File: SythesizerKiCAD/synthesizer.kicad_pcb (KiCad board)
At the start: 2 copper layers, 98.2 x 95.2 mm, 42 parts, among them U2 LM1877, U3 LM324A

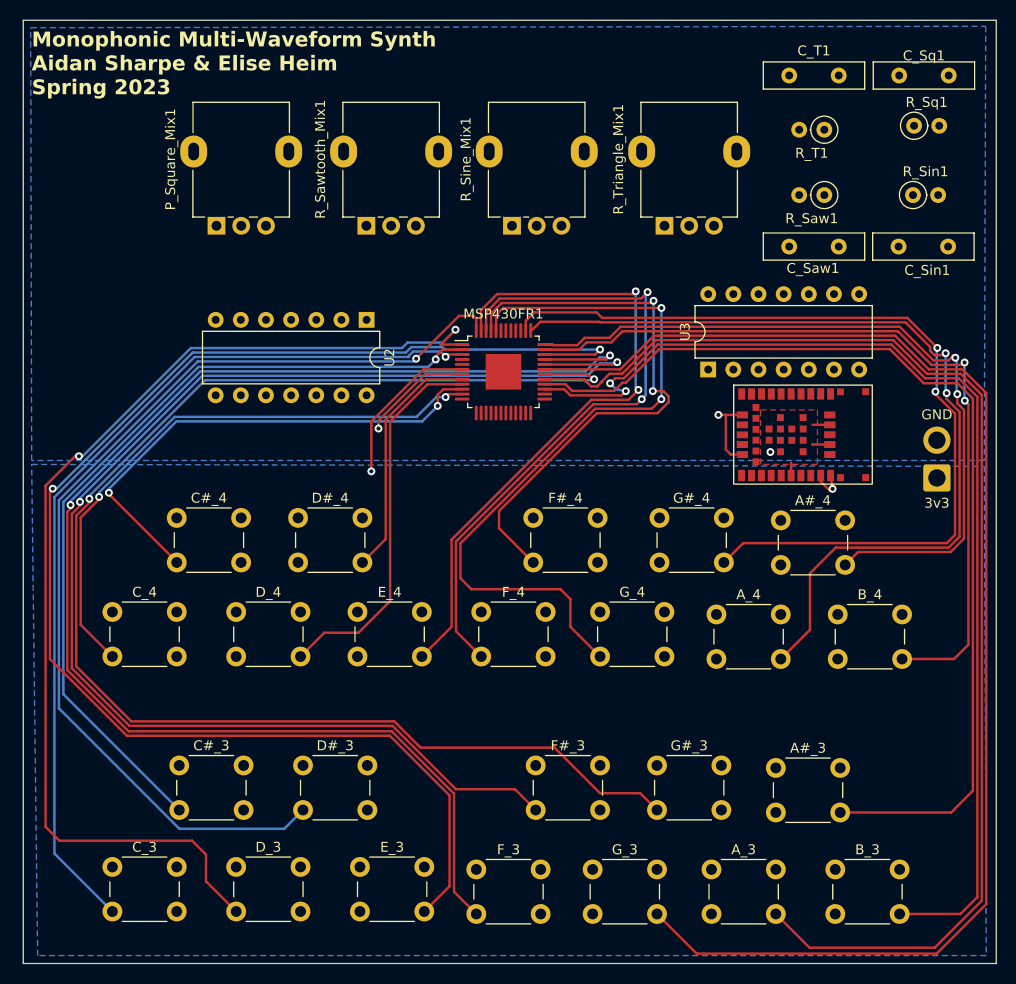
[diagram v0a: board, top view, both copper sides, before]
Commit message: Lowpass filters and isolators
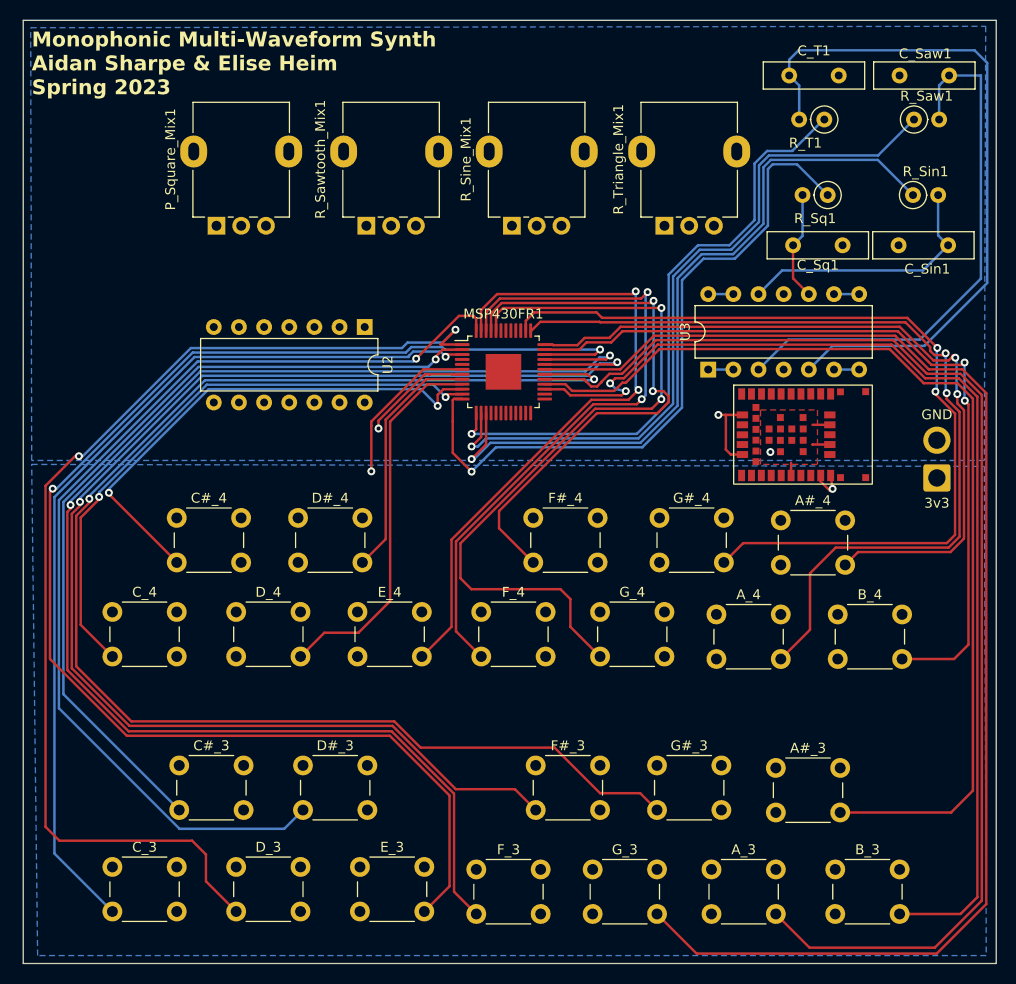
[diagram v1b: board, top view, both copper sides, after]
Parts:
- moved C_Saw1 23.6 mm to (121.2, 60.3), turned to 180 degrees
- moved C_Sq1 23.3 mm to (105.5, 77.5), turned to 0 degrees
- moved R_Saw1 11.8 mm to (117.7, 64.8), turned to 0 degrees
- moved R_Sq1 11.2 mm to (109.0, 72.4), turned to 180 degrees
- moved R_T1 1.03 mm to (108.6, 64.8)
- moved U2 0.75 mm to (62.2, 85.7)
- moved C_Sin1 0.13 mm to (121.1, 77.5)
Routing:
- net /Sine_PWM: track 0.00 -> 74.7 mm, vias 0 -> 1
- net /Sawtooth_PWM: track 0.00 -> 73.0 mm, vias 0 -> 1
- net /Triangle_Analog: track 0.00 -> 71.2 mm
- net /Square_PWM: track 0.00 -> 70.0 mm, vias 0 -> 1
- net /Triangle_PWM: track 0.00 -> 62.0 mm, vias 0 -> 1
- net /Sawtooth_Analog: track 0.00 -> 54.8 mm
- net /Sine_Analog: track 0.00 -> 26.7 mm
- net /Square_Analog: track 0.00 -> 11.1 mm
- net /Triangle_Isolated: track 0.00 -> 2.54 mm
- net /Square_Isolated: track 0.00 -> 2.54 mm
- net /Sine_Isolated: track 0.00 -> 2.54 mm
- net /Sawtooth_Isolated: track 0.00 -> 2.54 mm
- net /P2.5: track 50.8 -> 52.2 mm
- net /P2.4: track 59.5 -> 60.6 mm

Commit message: Volume, audio out, power in
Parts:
- removed GND: SolderWire-1sqmm_1x01_D1.4mm_OD2.7mm, Connector_Wire:SolderWire-1sqmm_1x01_D1.4mm_OD2.7mm
- added 9v1: Conn_01x01_Pin, Connector_Wire:SolderWire-0.1sqmm_1x01_D0.4mm_OD1mm, F.Cu at (29.8, 96.6)
- added Audio_Out1: Conn_01x01_Pin, Connector_Wire:SolderWire-0.1sqmm_1x01_D0.4mm_OD1mm, F.Cu at (30.0, 70.6)
- added GND1: Conn_01x01_Pin, Connector_Wire:SolderWire-0.1sqmm_1x01_D0.4mm_OD1mm, F.Cu at (29.8, 93.2)
- added GND2: Conn_01x01_Pin, Connector_Wire:SolderWire-0.1sqmm_1x01_D0.4mm_OD1mm, F.Cu at (30.0, 66.4)
- added R1: 100k, Resistor_THT:R_Axial_DIN0207_L6.3mm_D2.5mm_P2.54mm_Vertical, F.Cu at (87.8, 75.5)
- added R2: 300k, Resistor_THT:R_Axial_DIN0207_L6.3mm_D2.5mm_P2.54mm_Vertical, F.Cu at (91.0, 78.0)
- added R3: 300k, Resistor_THT:R_Axial_DIN0207_L6.3mm_D2.5mm_P2.54mm_Vertical, F.Cu at (42.7, 78.2)
- added R4: 100k, Resistor_THT:R_Axial_DIN0207_L6.3mm_D2.5mm_P2.54mm_Vertical, F.Cu at (39.5, 75.6)
- added R5: 300k, Resistor_THT:R_Axial_DIN0207_L6.3mm_D2.5mm_P2.54mm_Vertical, F.Cu at (74.9, 78.2)
- added R6: 100k, Resistor_THT:R_Axial_DIN0207_L6.3mm_D2.5mm_P2.54mm_Vertical, F.Cu at (71.7, 75.6)
- added R7: 300k, Resistor_THT:R_Axial_DIN0207_L6.3mm_D2.5mm_P2.54mm_Vertical, F.Cu at (58.8, 78.3)
- added R8: 100k, Resistor_THT:R_Axial_DIN0207_L6.3mm_D2.5mm_P2.54mm_Vertical, F.Cu at (55.7, 75.7)
- added R9: 100k, Resistor_THT:R_Axial_DIN0207_L6.3mm_D2.5mm_P2.54mm_Vertical, F.Cu at (33.1, 74.6)
- added R_Volume1: R_Potentiometer_US, Potentiometer_THT:Potentiometer_Alpha_RD901F-40-00D_Single_Vertical, F.Cu at (32.1, 89.9)
- 3v3: value SolderWire-1sqmm_1x01_D1.4mm_OD2.7mm -> Conn_01x01_Pin; footprint Connector_Wire:SolderWire-1sqmm_1x01_D1.4mm_OD2.7mm -> Connector_Wire:SolderWire-0.1sqmm_1x01_D0.4mm_OD1mm
- U3: value LM324A -> LMC6484
- moved 3v3 90.2 mm to (29.8, 103.0)
- moved P_Square_Mix1 46.2 mm to (93.4, 73.2)
- moved R_Sine_Mix1 32.1 mm to (45.1, 73.3)
- moved R_Triangle_Mix1 15.4 mm to (77.3, 73.2)
- moved R_Sawtooth_Mix1 2.40 mm to (61.2, 73.4)
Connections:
- P_Square_Mix1 pad 1: unconnected-(P_Square_Mix1-Pad1) -> /Square_Divided
- P_Square_Mix1 pad 2: unconnected-(P_Square_Mix1-Pad2) -> /Mixed
- R_Sawtooth_Mix1 pad 1: unconnected-(R_Sawtooth_Mix1-Pad1) -> /Sawtooth_Divided
- R_Sawtooth_Mix1 pad 2: unconnected-(R_Sawtooth_Mix1-Pad2) -> /Mixed
- R_Sine_Mix1 pad 1: unconnected-(R_Sine_Mix1-Pad1) -> /Sine_Divided
- R_Sine_Mix1 pad 2: unconnected-(R_Sine_Mix1-Pad2) -> /Mixed
- R_Triangle_Mix1 pad 1: unconnected-(R_Triangle_Mix1-Pad1) -> /Triangle_Divided
- R_Triangle_Mix1 pad 2: unconnected-(R_Triangle_Mix1-Pad2) -> /Mixed
- U1 pad 42: /GND -> (no net)
- U2 pad 14: /12v -> /9v
- U2 pad 2: unconnected-(U2-Pad2) -> /Audio_Out
- U2 pad 6: unconnected-(U2A-+-Pad6) -> /Mixed
- U2 pad 7: unconnected-(U2A---Pad7) -> Net-(U2A--)
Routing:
- net /Mixed: track 0.00 -> 67.6 mm
- net /Sine_Isolated: track 2.54 -> 58.5 mm
- net /Sawtooth_Isolated: track 2.54 -> 55.0 mm, vias 0 -> 1
- net /Triangle_Isolated: track 2.54 -> 51.6 mm, vias 0 -> 1
- net /Audio_Out: track 0.00 -> 48.1 mm
- net /9v: track 0.00 -> 34.0 mm
- net Net-(U2A--): track 0.00 -> 31.0 mm
- net /Square_Isolated: track 2.54 -> 24.7 mm
- net /GND: track 23.4 -> 36.0 mm, vias 3 -> 5
- net /Sawtooth_Analog: track 54.8 -> 47.2 mm
- net /Square_Divided: track 0.00 -> 6.57 mm
- net /Sine_Divided: track 0.00 -> 6.57 mm
- net /Triangle_Divided: track 0.00 -> 6.57 mm
- net /Sawtooth_Divided: track 0.00 -> 6.46 mm
- net unconnected-(U1-GPI_15-Pad15): track 0.00 -> 5.20 mm
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
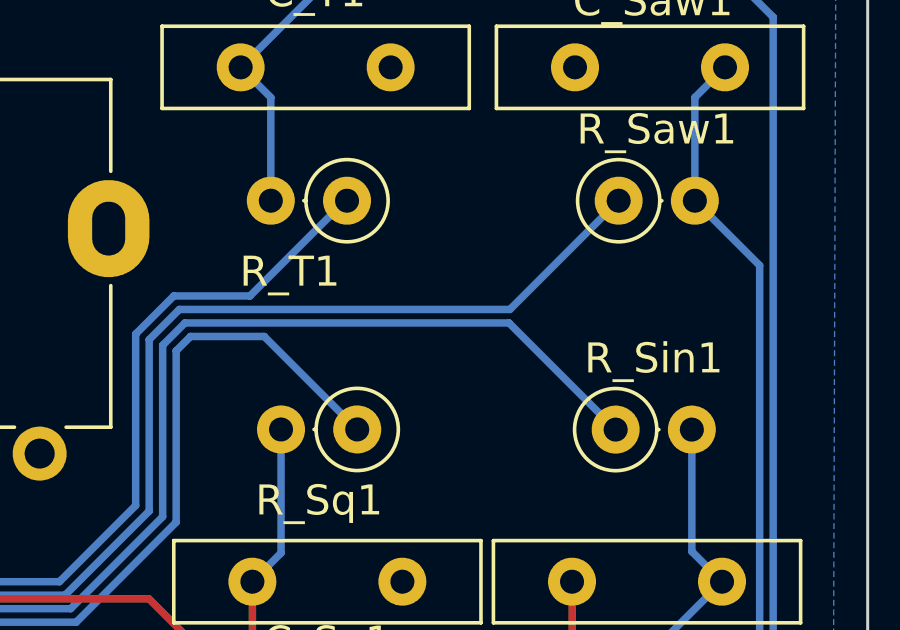
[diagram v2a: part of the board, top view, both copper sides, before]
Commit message: Fixed ground issue
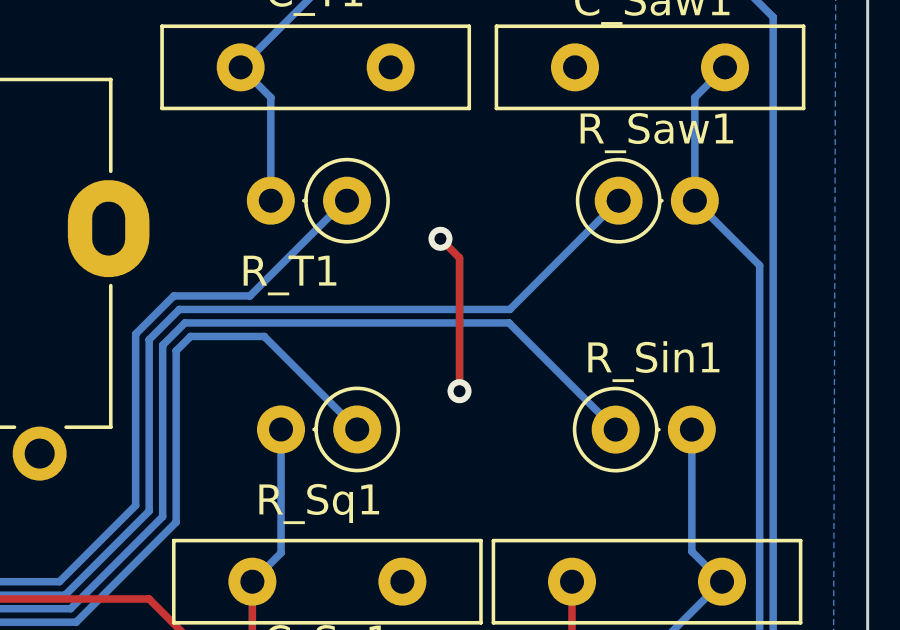
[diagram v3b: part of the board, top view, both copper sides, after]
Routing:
- net /GND: track 36.0 -> 41.4 mm, vias 5 -> 7
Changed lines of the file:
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@@
   (segment (start 71.03 90.5) (end 71.04 90.51) (width 0.25) (layer "F.Cu") (net 31))
   (segment (start 108.95 95.6) (end 107.45 95.6) (width 0.25) (layer "F.Cu") (net 31))
+  (segment (start 111.76 66.04) (end 112.395 66.675) (width 0.25) (layer "F.Cu") (net 31))
   (segment (start 98.7 94.6) (end 97.95 94.6) (width 0.25) (layer "F.Cu") (net 31))
+  (segment (start 112.395 66.675) (end 112.395 71.12) (width 0.25) (layer "F.Cu") (net 31))
   (segment (start 68.7 90.5) (end 68.8 90.5) (width 0.25) (layer "F.Cu") (net 31))
   (segment (start 116.145 82.345) (end 117 83) (width 0.25) (layer "F.Cu") (net 31))
@@
   (segment (start 99.2 98.6) (end 98.7 98.1) (width 0.25) (layer "F.Cu") (net 31))
   (segment (start 117 83) (end 116.8 83) (width 0.25) (layer "F.Cu") (net 31))
+  (via (at 111.76 66.04) (size 0.8) (drill 0.4) (layers "F.Cu" "B.Cu") (free) (net 31))
   (via (at 122.2 86) (size 0.8) (drill 0.4) (layers "F.Cu" "B.Cu") (free) (net 31))
+  (via (at 112.395 71.12) (size 0.8) (drill 0.4) (layers "F.Cu" "B.Cu") (free) (net 31))
   (via (at 97.95 94.6) (size 0.8) (drill 0.4) (layers "F.Cu" "B.Cu") (net 31))
   (via (at 63.6255 95.9745) (size 0.8) (drill 0.4) (layers "F.Cu" "B.Cu") (net 31))

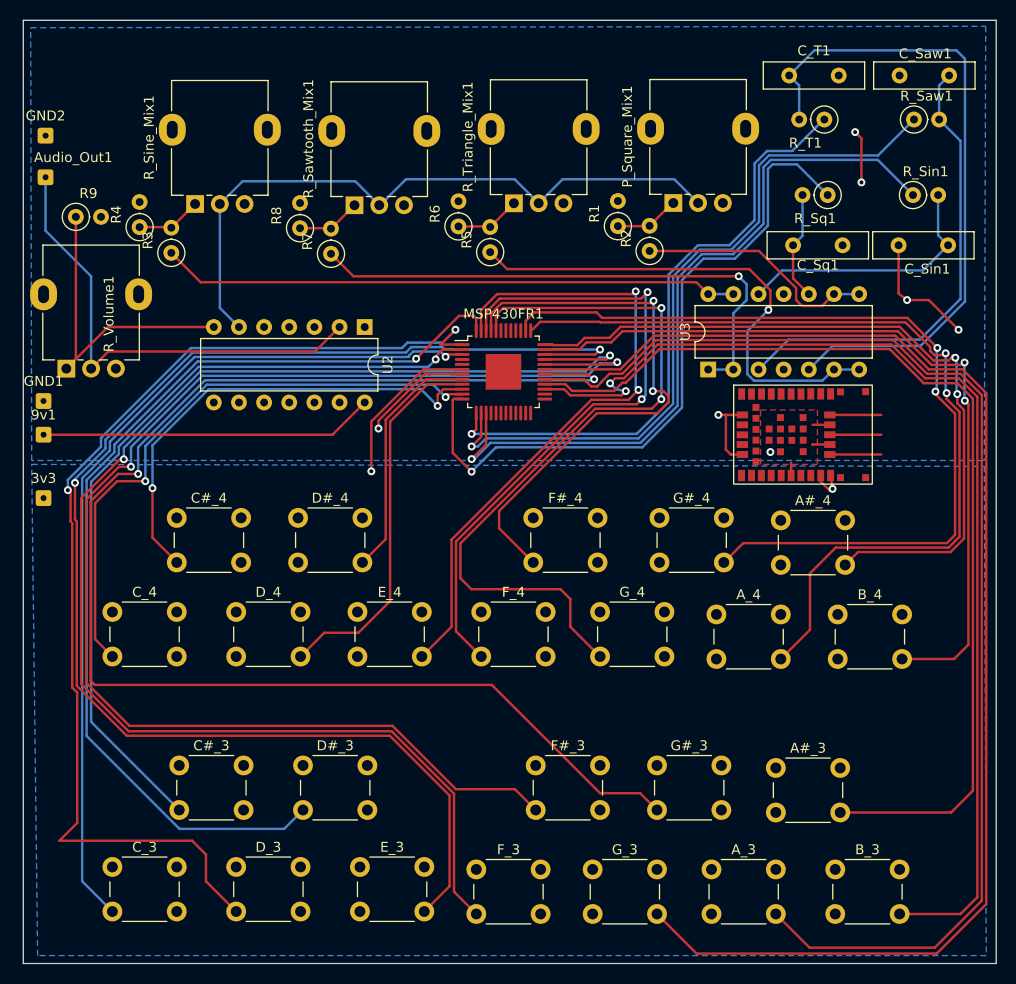
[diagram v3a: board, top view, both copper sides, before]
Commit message: Removed NINA, breakouts for MSP, extra pads
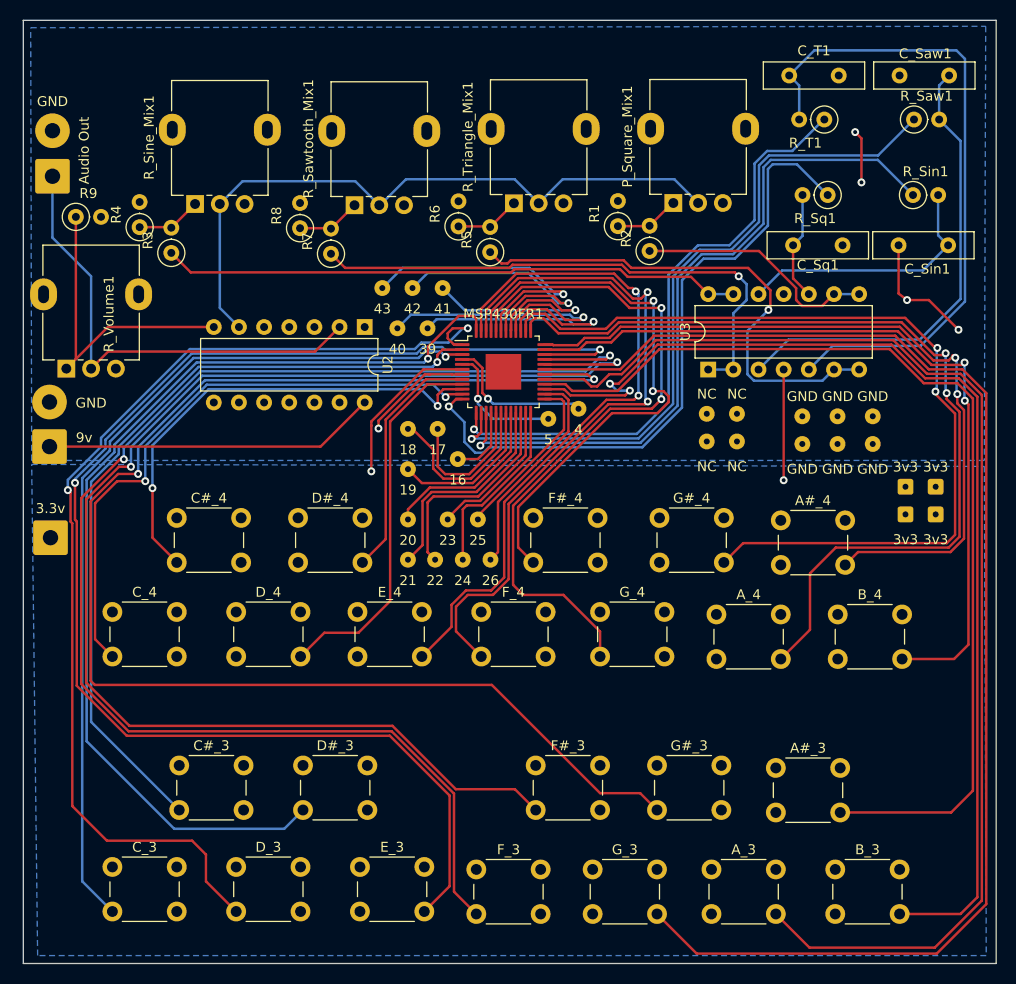
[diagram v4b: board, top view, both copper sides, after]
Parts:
- removed the 3v3 at (29.8, 103.0)
- removed 9v1, Audio_Out1, GND1, GND2: Conn_01x01_Pin, Connector_Wire:SolderWire-0.1sqmm_1x01_D0.4mm_OD1mm
- removed U1: ~, Library:NINA-W156-Correct-Pads
- added 16: SolderWire-0.1sqmm_1x01_D0.4mm_OD1mm, Connector_Wire:SolderWire-0.1sqmm_1x01_D0.4mm_OD1mm, F.Cu at (71.6, 99.1)
- added 17: SolderWire-0.1sqmm_1x01_D0.4mm_OD1mm, Connector_Wire:SolderWire-0.1sqmm_1x01_D0.4mm_OD1mm, F.Cu at (69.6, 96.0)
- added 18: SolderWire-0.1sqmm_1x01_D0.4mm_OD1mm, Connector_Wire:SolderWire-0.1sqmm_1x01_D0.4mm_OD1mm, F.Cu at (66.6, 96.0)
- added 19: SolderWire-0.1sqmm_1x01_D0.4mm_OD1mm, Connector_Wire:SolderWire-0.1sqmm_1x01_D0.4mm_OD1mm, F.Cu at (66.6, 100.1)
- added 20: SolderWire-0.1sqmm_1x01_D0.4mm_OD1mm, Connector_Wire:SolderWire-0.1sqmm_1x01_D0.4mm_OD1mm, F.Cu at (66.6, 105.2)
- added 21: SolderWire-0.1sqmm_1x01_D0.4mm_OD1mm, Connector_Wire:SolderWire-0.1sqmm_1x01_D0.4mm_OD1mm, F.Cu at (66.6, 109.2)
- added 22: SolderWire-0.1sqmm_1x01_D0.4mm_OD1mm, Connector_Wire:SolderWire-0.1sqmm_1x01_D0.4mm_OD1mm, F.Cu at (69.3, 109.2)
- added 23: SolderWire-0.1sqmm_1x01_D0.4mm_OD1mm, Connector_Wire:SolderWire-0.1sqmm_1x01_D0.4mm_OD1mm, F.Cu at (70.6, 105.2)
- added 24: SolderWire-0.1sqmm_1x01_D0.4mm_OD1mm, Connector_Wire:SolderWire-0.1sqmm_1x01_D0.4mm_OD1mm, F.Cu at (72.1, 109.2)
- added 25: SolderWire-0.1sqmm_1x01_D0.4mm_OD1mm, Connector_Wire:SolderWire-0.1sqmm_1x01_D0.4mm_OD1mm, F.Cu at (73.7, 105.2)
- added 26: SolderWire-0.1sqmm_1x01_D0.4mm_OD1mm, Connector_Wire:SolderWire-0.1sqmm_1x01_D0.4mm_OD1mm, F.Cu at (74.9, 109.2)
- added 3.3v: SolderWire-0.75sqmm_1x01_D1.25mm_OD3.5mm, Connector_Wire:SolderWire-0.75sqmm_1x01_D1.25mm_OD3.5mm, F.Cu at (30.5, 107.0)
- added 39: SolderWire-0.1sqmm_1x01_D0.4mm_OD1mm, Connector_Wire:SolderWire-0.1sqmm_1x01_D0.4mm_OD1mm, F.Cu at (68.6, 85.9)
- added 3v3: SolderWire-0.1sqmm_1x01_D0.4mm_OD1mm, Connector_Wire:SolderWire-0.1sqmm_1x01_D0.4mm_OD1mm, F.Cu at (116.8, 101.9)
- added 3v3: SolderWire-0.1sqmm_1x01_D0.4mm_OD1mm, Connector_Wire:SolderWire-0.1sqmm_1x01_D0.4mm_OD1mm, F.Cu at (116.8, 104.6)
- added 3v3: SolderWire-0.1sqmm_1x01_D0.4mm_OD1mm, Connector_Wire:SolderWire-0.1sqmm_1x01_D0.4mm_OD1mm, F.Cu at (119.9, 104.6)
- added 3v3: SolderWire-0.1sqmm_1x01_D0.4mm_OD1mm, Connector_Wire:SolderWire-0.1sqmm_1x01_D0.4mm_OD1mm, F.Cu at (119.9, 101.9)
- added 4: SolderWire-0.1sqmm_1x01_D0.4mm_OD1mm, Connector_Wire:SolderWire-0.1sqmm_1x01_D0.4mm_OD1mm, F.Cu at (83.8, 94.0)
- added 40: SolderWire-0.1sqmm_1x01_D0.4mm_OD1mm, Connector_Wire:SolderWire-0.1sqmm_1x01_D0.4mm_OD1mm, F.Cu at (65.5, 85.9)
- added 41: SolderWire-0.1sqmm_1x01_D0.4mm_OD1mm, Connector_Wire:SolderWire-0.1sqmm_1x01_D0.4mm_OD1mm, F.Cu at (70.1, 81.8)
- added 42: SolderWire-0.1sqmm_1x01_D0.4mm_OD1mm, Connector_Wire:SolderWire-0.1sqmm_1x01_D0.4mm_OD1mm, F.Cu at (67.1, 81.8)
- added 43: SolderWire-0.1sqmm_1x01_D0.4mm_OD1mm, Connector_Wire:SolderWire-0.1sqmm_1x01_D0.4mm_OD1mm, F.Cu at (64.0, 81.8)
- added 5: SolderWire-0.1sqmm_1x01_D0.4mm_OD1mm, Connector_Wire:SolderWire-0.1sqmm_1x01_D0.4mm_OD1mm, F.Cu at (80.8, 95.0)
- added 9v: SolderWire-0.75sqmm_1x01_D1.25mm_OD3.5mm, Connector_Wire:SolderWire-0.75sqmm_1x01_D1.25mm_OD3.5mm, F.Cu at (30.4, 97.8)
- added Audio Out: SolderWire-0.75sqmm_1x01_D1.25mm_OD3.5mm, Connector_Wire:SolderWire-0.75sqmm_1x01_D1.25mm_OD3.5mm, F.Cu at (30.7, 70.5)
- added GND: SolderWire-0.1sqmm_1x01_D0.4mm_OD1mm, Connector_Wire:SolderWire-0.1sqmm_1x01_D0.4mm_OD1mm, F.Cu at (110.0, 94.7)
- added GND: SolderWire-0.1sqmm_1x01_D0.4mm_OD1mm, Connector_Wire:SolderWire-0.1sqmm_1x01_D0.4mm_OD1mm, F.Cu at (113.5, 97.5)
- added GND: SolderWire-0.1sqmm_1x01_D0.4mm_OD1mm, Connector_Wire:SolderWire-0.1sqmm_1x01_D0.4mm_OD1mm, F.Cu at (106.4, 97.5)
- added GND: SolderWire-0.1sqmm_1x01_D0.4mm_OD1mm, Connector_Wire:SolderWire-0.1sqmm_1x01_D0.4mm_OD1mm, F.Cu at (110.0, 97.5)
- added GND: SolderWire-0.75sqmm_1x01_D1.25mm_OD3.5mm, Connector_Wire:SolderWire-0.75sqmm_1x01_D1.25mm_OD3.5mm, F.Cu at (30.7, 65.9)
- added GND: SolderWire-0.1sqmm_1x01_D0.4mm_OD1mm, Connector_Wire:SolderWire-0.1sqmm_1x01_D0.4mm_OD1mm, F.Cu at (106.4, 94.7)
- added GND: SolderWire-0.75sqmm_1x01_D1.25mm_OD3.5mm, Connector_Wire:SolderWire-0.75sqmm_1x01_D1.25mm_OD3.5mm, F.Cu at (30.4, 93.3)
- added GND: SolderWire-0.1sqmm_1x01_D0.4mm_OD1mm, Connector_Wire:SolderWire-0.1sqmm_1x01_D0.4mm_OD1mm, F.Cu at (113.5, 94.7)
- added NC: SolderWire-0.1sqmm_1x01_D0.4mm_OD1mm, Connector_Wire:SolderWire-0.1sqmm_1x01_D0.4mm_OD1mm, F.Cu at (99.8, 94.5)
- added NC: SolderWire-0.1sqmm_1x01_D0.4mm_OD1mm, Connector_Wire:SolderWire-0.1sqmm_1x01_D0.4mm_OD1mm, F.Cu at (96.8, 94.5)
- added NC: SolderWire-0.1sqmm_1x01_D0.4mm_OD1mm, Connector_Wire:SolderWire-0.1sqmm_1x01_D0.4mm_OD1mm, F.Cu at (96.8, 97.3)
- added NC: SolderWire-0.1sqmm_1x01_D0.4mm_OD1mm, Connector_Wire:SolderWire-0.1sqmm_1x01_D0.4mm_OD1mm, F.Cu at (99.8, 97.3)
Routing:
- net unconnected-(MSP430FR1-P5.0/TB2.1/MFM.RX/A8-Pad43): track 0.00 -> 29.3 mm, vias 0 -> 1
- net unconnected-(MSP430FR1-P5.3/TB2TRG/A11-Pad40): track 0.00 -> 28.9 mm, vias 0 -> 1
- net unconnected-(MSP430FR1-P5.4-Pad39): track 0.00 -> 27.1 mm, vias 0 -> 1
- net unconnected-(MSP430FR1-P5.1/TB2.2/MFM.TX/A9-Pad42): track 0.00 -> 26.6 mm, vias 0 -> 1
- net unconnected-(MSP430FR1-P5.2/TB2CLK/A10-Pad41): track 0.00 -> 23.4 mm, vias 0 -> 1
- net unconnected-(MSP430FR1-P4.0/UCA1STE/ISOTXD/ISORXD-Pad26): track 0.00 -> 22.0 mm
- net unconnected-(MSP430FR1-P6.1/TB3.2-Pad21): track 0.00 -> 22.0 mm
- net unconnected-(MSP430FR1-P6.0/TB3.1-Pad22): track 0.00 -> 21.7 mm
- net /UART_MSP_RX: track 0.00 -> 18.5 mm
- net unconnected-(MSP430FR1-P6.2/TB3.3-Pad20): track 0.00 -> 17.7 mm
- net unconnected-(MSP430FR1-P4.1/UCA1CLK-Pad25): track 0.00 -> 17.6 mm
- net unconnected-(MSP430FR1-P6.4/TB3.5-Pad18): track 0.00 -> 17.4 mm
- net unconnected-(MSP430FR1-P6.3/TB3.4-Pad19): track 0.00 -> 15.6 mm
- net unconnected-(MSP430FR1-TEST/SBWTCK-Pad4): track 0.00 -> 15.3 mm, vias 0 -> 1
- net /UART_MSP_TX: track 0.00 -> 14.9 mm
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- removed copper zone on F.Cu, net /GND
